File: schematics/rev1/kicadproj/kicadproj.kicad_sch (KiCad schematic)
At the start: 53 parts, among them Q1 FQP47P06, Q2 FQP27P06, SW1 WAKE Switch, SW2 SET 15MIN, SW3 LOUD, SW4 NIGHT, U2 ATmega328P-PU

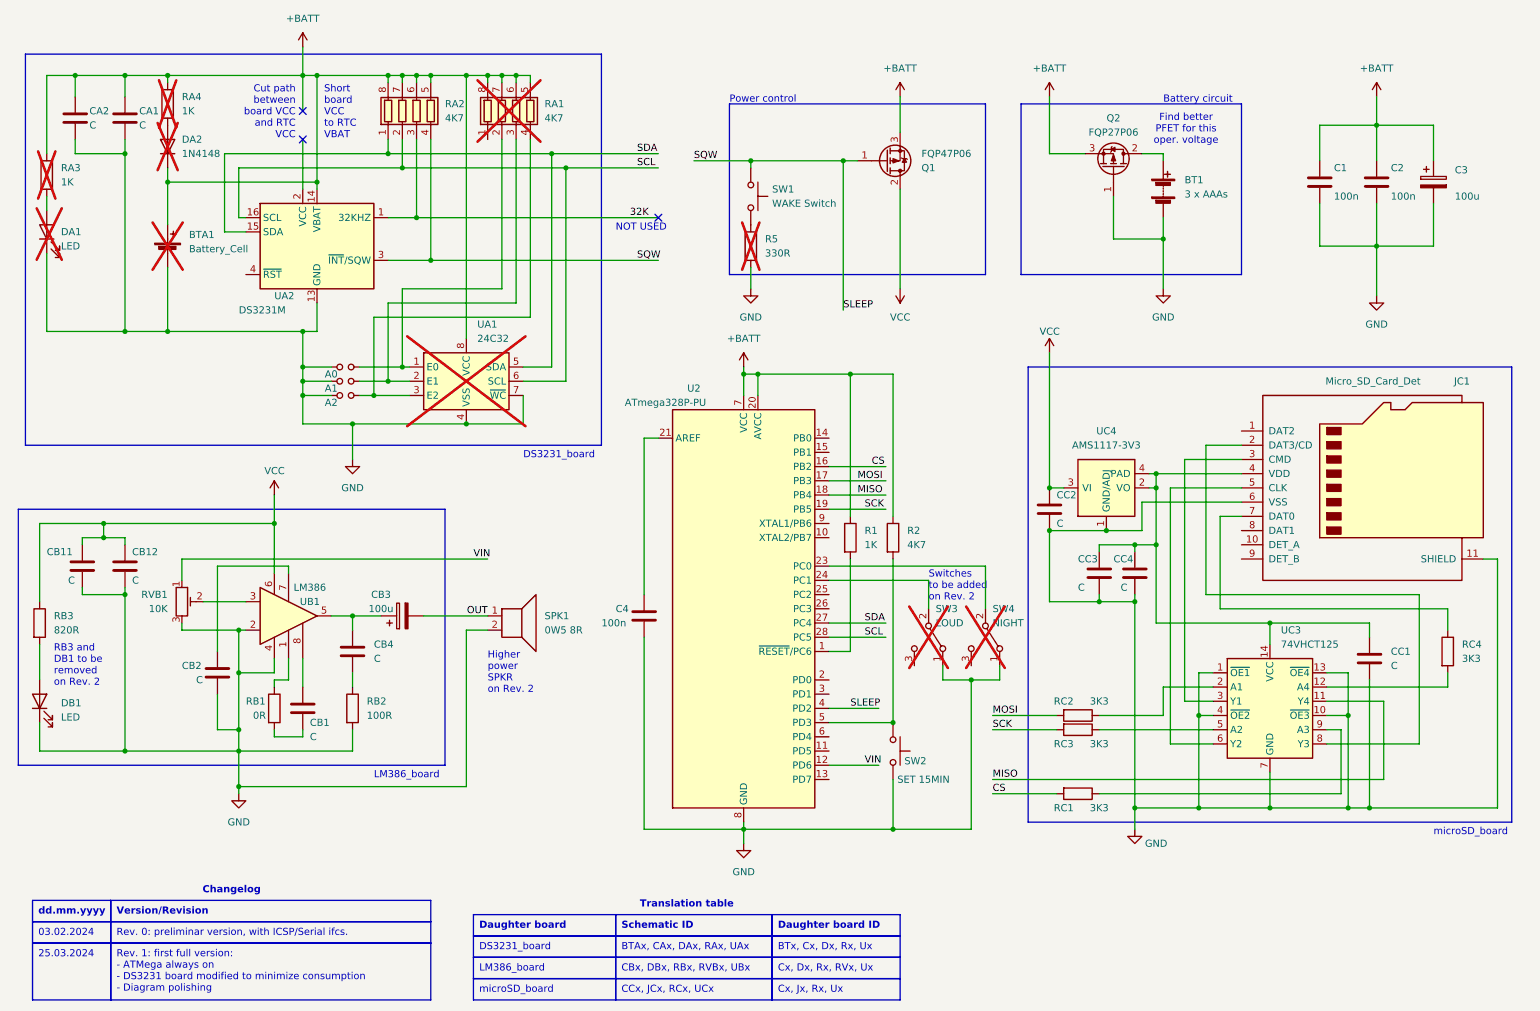
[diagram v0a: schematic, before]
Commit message: Updated schematic with new low-Vgs PFETs and cap on LM386 supply
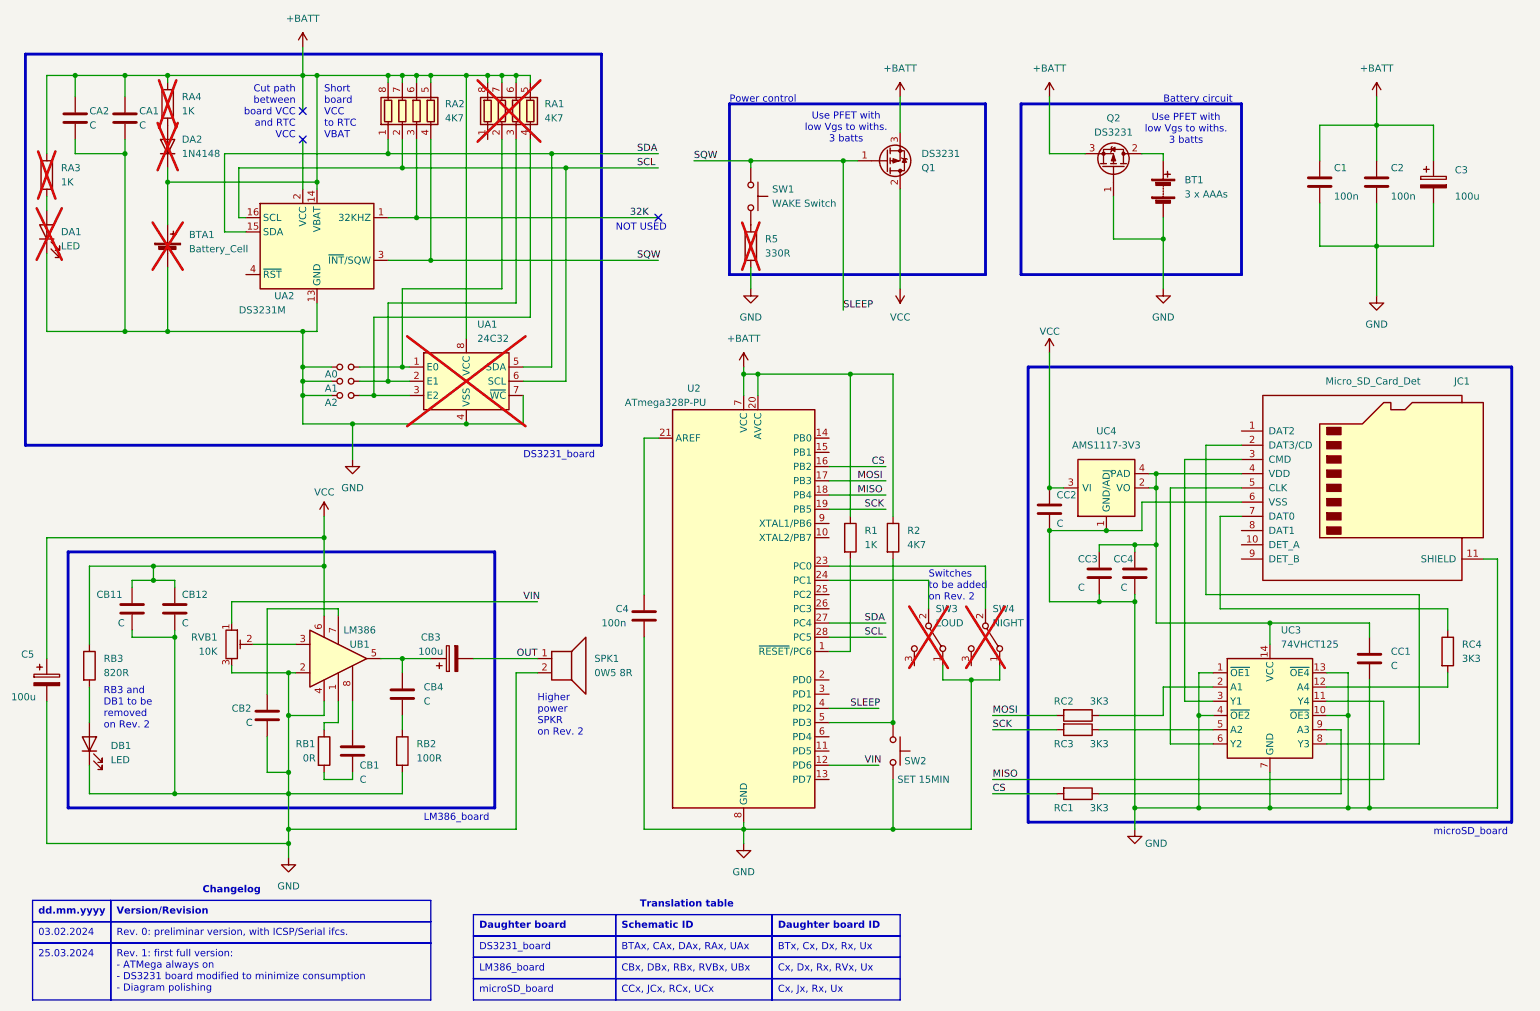
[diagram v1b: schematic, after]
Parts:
- added C5: 100u, symbol Device:CP
- Q1: value FQP47P06 -> DS3231
- Q2: value FQP27P06 -> DS3231
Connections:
- net GND: now also C5.2
- net VCC: now also C5.1
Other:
- note added: "Use PFET with low Vgs to withs. 3 batts"
- note removed: "Find better PFET for this oper. voltage"
- moved on the sheet: CB1, CB11, CB12, CB2, CB3, CB4, DB1, RB1, RB2, RB3, RVB1, SPK1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
